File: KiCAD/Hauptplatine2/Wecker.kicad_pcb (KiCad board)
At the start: 2 copper layers, 45 parts, among them IC1 ATMEGA328P-P, P1 CONN_5V, P10 LED_Bild2, P11 CONN_MP3, P2 CONN_MP3Player, P3 LED_Bild1, P4 CONN_TASTER, P5 CONN_DREHENCODER, P6 CONN_DISPLAY, P7 CONN_01X02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

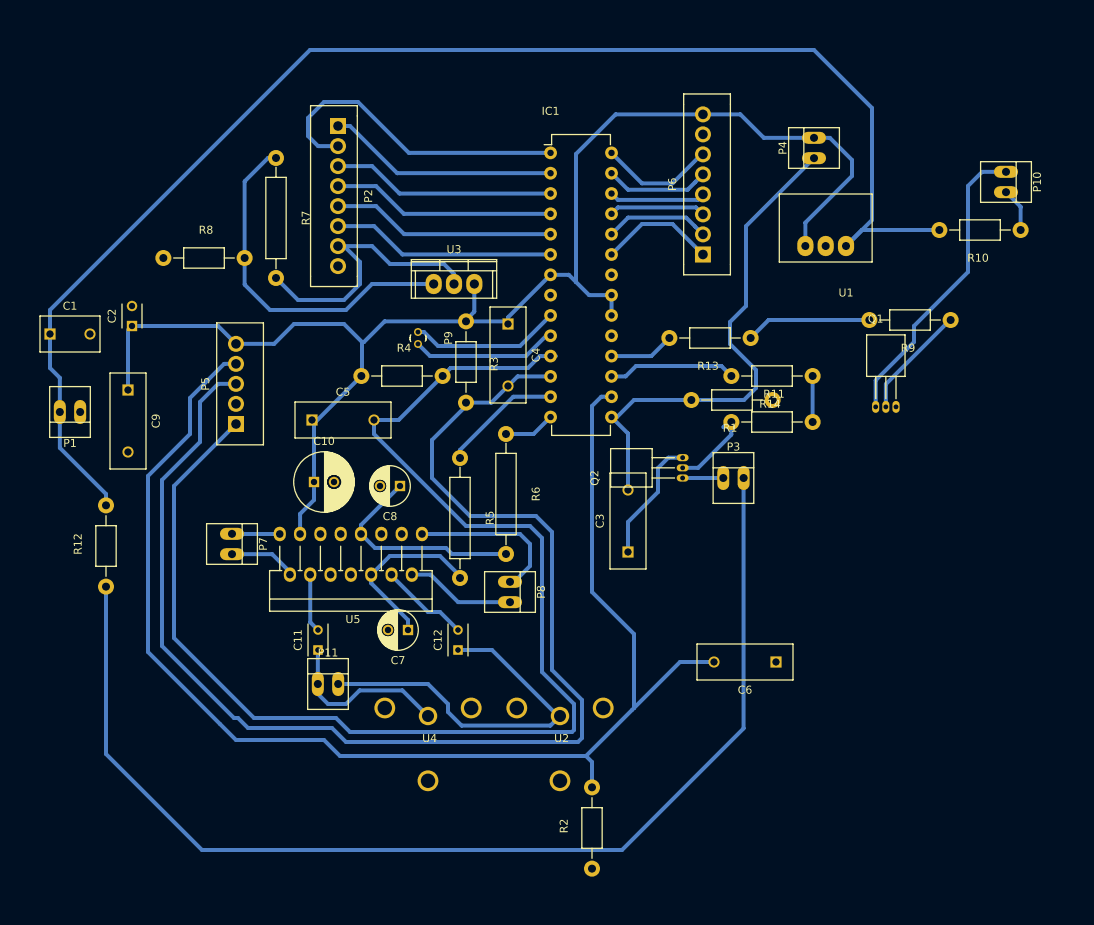
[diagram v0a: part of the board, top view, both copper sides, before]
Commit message: PCB enger gepackt. MP3 Player in Code eingebunden.
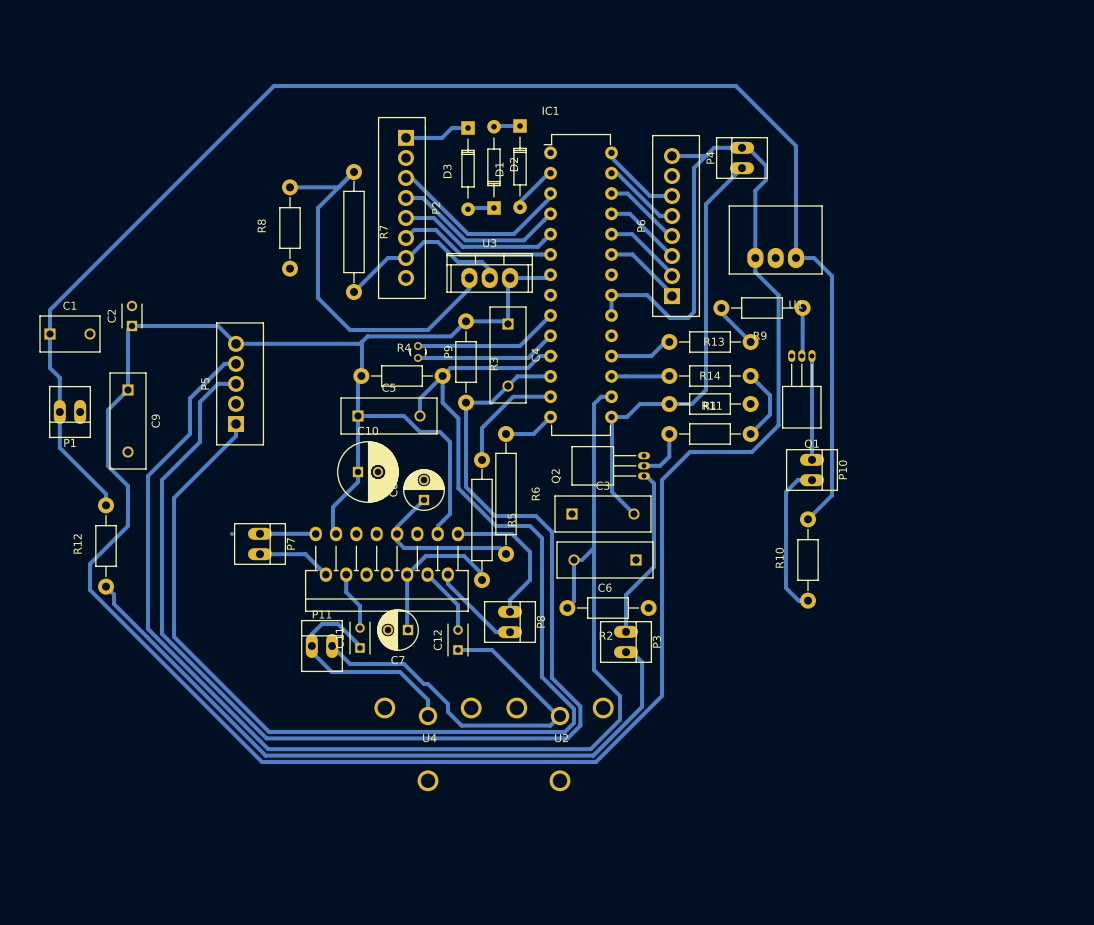
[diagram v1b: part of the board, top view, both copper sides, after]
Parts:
- added D1: D, Diodes_ThroughHole:Diode_DO-35_SOD27_Horizontal_RM10, F.Cu at (131.5, 53.2)
- added D2: D, Diodes_ThroughHole:Diode_DO-35_SOD27_Horizontal_RM10, F.Cu at (128.2, 63.5)
- added D3: D, Diodes_ThroughHole:Diode_DO-35_SOD27_Horizontal_RM10, F.Cu at (125.0, 53.5)
- moved R10 46.5 mm to (167.5, 107.5), turned to 90 degrees
- moved P10 43.4 mm to (168.0, 96.2)
- moved R2 27.6 mm to (142.5, 113.5), turned to 180 degrees
- moved P3 24.5 mm to (144.8, 117.8), turned to 270 degrees
- moved C6 21.7 mm to (146.0, 107.5)
- moved R9 18.6 mm to (161.8, 76.0)
- moved R8 11.4 mm to (102.8, 66.0), turned to 90 degrees
- moved Q1 10.2 mm to (168.0, 82.0), turned to 180 degrees
- moved R7 9.91 mm to (110.8, 66.5)
- moved P4 9.09 mm to (159.2, 57.2)
- moved P2 8.63 mm to (117.2, 54.7)
- moved C3 8.46 mm to (138.0, 101.8), turned to 0 degrees
- moved R11 7.89 mm to (155.2, 91.8)
- moved R14 7.75 mm to (155.2, 84.5)
- moved P6 6.48 mm to (150.5, 74.5)
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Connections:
- IC1 pad 1: MP3-ON2 -> Net-(IC1-Pad1)
- P2 pad 1: MP3-ON1 -> Net-(D3-Pad1)
- P2 pad 2: MP3-ON2 -> Net-(P2-Pad2)
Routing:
- net DE-E: track 180.0 -> 359.1 mm
- net Net-(P3-Pad2): track 144.5 -> 87.1 mm
- net MP3-ON2: track 40.3 -> 0.00 mm
- net Net-(P10-Pad1): track 38.1 -> 13.0 mm
- net MP3-ON1: track 29.0 -> 5.97 mm
- net Net-(P3-Pad1): track 5.08 -> 21.6 mm
- net DE-C: track 15.7 -> 0.11 mm
- net Net-(P10-Pad2): track 5.49 -> 19.3 mm
- net MP3-VCC: track 36.0 -> 22.8 mm
- net DE-D: track 169.6 -> 158.1 mm
- net Net-(R13-Pad1): track 15.8 -> 5.77 mm
- net LED-Bild1: track 16.0 -> 7.25 mm
- net MP3-T5: track 28.0 -> 19.8 mm
- net Net-(D3-Pad1): track 0.00 -> 8.26 mm
- net Net-(Q1-Pad2): track 14.3 -> 6.04 mm
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
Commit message: Haupptlatine2 fertig, Masseflächen vergrößert, Leiterbahnen zusammengeschoben
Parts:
- moved P1 98.2 mm to (167.0, 54.0), turned to 0 degrees
- moved C1 98.2 mm to (169.2, 61.2), turned to 180 degrees
- moved C2 84.5 mm to (150.5, 129.0), turned to 0 degrees
- moved R12 72.5 mm to (150.2, 122.8), turned to 0 degrees
- moved C9 71.7 mm to (151.2, 106.5), turned to 0 degrees
- moved P5 70.3 mm to (160.8, 117.8), turned to 270 degrees
- moved R10 10.4 mm to (159.2, 101.2), turned to 180 degrees
- moved P7 8.90 mm to (104.5, 98.5), turned to 180 degrees
- moved U4 2.51 mm to (117.5, 127.2)
- moved U1 1.25 mm to (166.0, 71.0)
- moved C5 1.00 mm to (112.2, 89.5)
- moved R2 1.00 mm to (143.5, 113.5)
- moved P4 0.56 mm to (158.8, 57.5)
- moved U2 0.50 mm to (136.0, 127.0)
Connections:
- P5 pad 1: DE-A -> DE-C
- P5 pad 2: DE-C -> DE-A
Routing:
- net +5V: track 186.4 -> 80.9 mm
- net Net-(P3-Pad2): track 87.1 -> 4.66 mm
- net DE-D: track 158.1 -> 84.9 mm
- net DE-B: track 156.1 -> 98.5 mm
- net DE-A: track 159.2 -> 116.5 mm
- net DE-E: track 359.1 -> 384.5 mm
- net Net-(P10-Pad2): track 19.3 -> 5.25 mm
- net SPK-R-: track 9.30 -> 13.9 mm
- net MP3-L: track 29.2 -> 26.2 mm
- net MP3-R: track 50.0 -> 52.5 mm
- net T1.1: track 57.3 -> 59.2 mm
- net Amp-Mute: track 14.2 -> 15.5 mm
- net SPK-R+: track 6.98 -> 5.86 mm
- net Net-(R7-Pad1): track 50.5 -> 49.4 mm
- net DE-C: track 0.11 -> 1.00 mm
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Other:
- board outline added: 77.5 x 90.2 mm
- rule trace_min: 0.2 -> 0.5

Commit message: Doku erweitert
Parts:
- moved C9 50.6 mm to (104.8, 86.5), turned to 90 degrees
- moved C2 42.2 mm to (162.2, 88.5)
- moved Q1 28.9 mm to (153.5, 107.0), turned to 90 degrees
- moved R9 28.5 mm to (162.8, 104.5), turned to 0 degrees
- moved P3 27.8 mm to (165.5, 99.2)
- moved R12 22.1 mm to (154.0, 101.0), turned to 180 degrees
- moved P4 21.8 mm to (151.2, 78.0)
- moved P10 13.4 mm to (165.8, 109.5)
- moved C1 13.1 mm to (165.2, 73.8)
- moved U1 12.8 mm to (167.5, 83.8)
- moved R10 11.7 mm to (152.8, 111.0)
- moved C6 10.5 mm to (135.5, 107.5), turned to 0 degrees
- moved P1 7.74 mm to (160.0, 57.2)
- moved P5 6.17 mm to (155.0, 120.0), turned to 180 degrees
- moved R13 4.42 mm to (152.0, 83.2)
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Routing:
- net DE-E: track 384.5 -> 291.6 mm
- net DE-D: track 84.9 -> 54.6 mm
- net Net-(R13-Pad1): track 5.77 -> 29.2 mm
- net T1.1: track 59.2 -> 36.8 mm
- net DE-A: track 116.5 -> 95.7 mm
- net DE-B: track 98.5 -> 78.9 mm
- net +5V: track 80.9 -> 95.0 mm
- net Net-(P10-Pad2): track 5.25 -> 13.4 mm
- net LED-Bild2: track 8.17 -> 4.49 mm
- net Net-(C7-Pad1): track 18.6 -> 21.7 mm
- net Net-(Q2-Pad2): track 6.48 -> 4.27 mm
- net LED-Bild1: track 7.25 -> 5.18 mm
- net Net-(P3-Pad2): track 4.66 -> 6.62 mm
- net Net-(Q1-Pad2): track 6.04 -> 4.68 mm
- net DISP-SCL: track 9.91 -> 8.62 mm
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
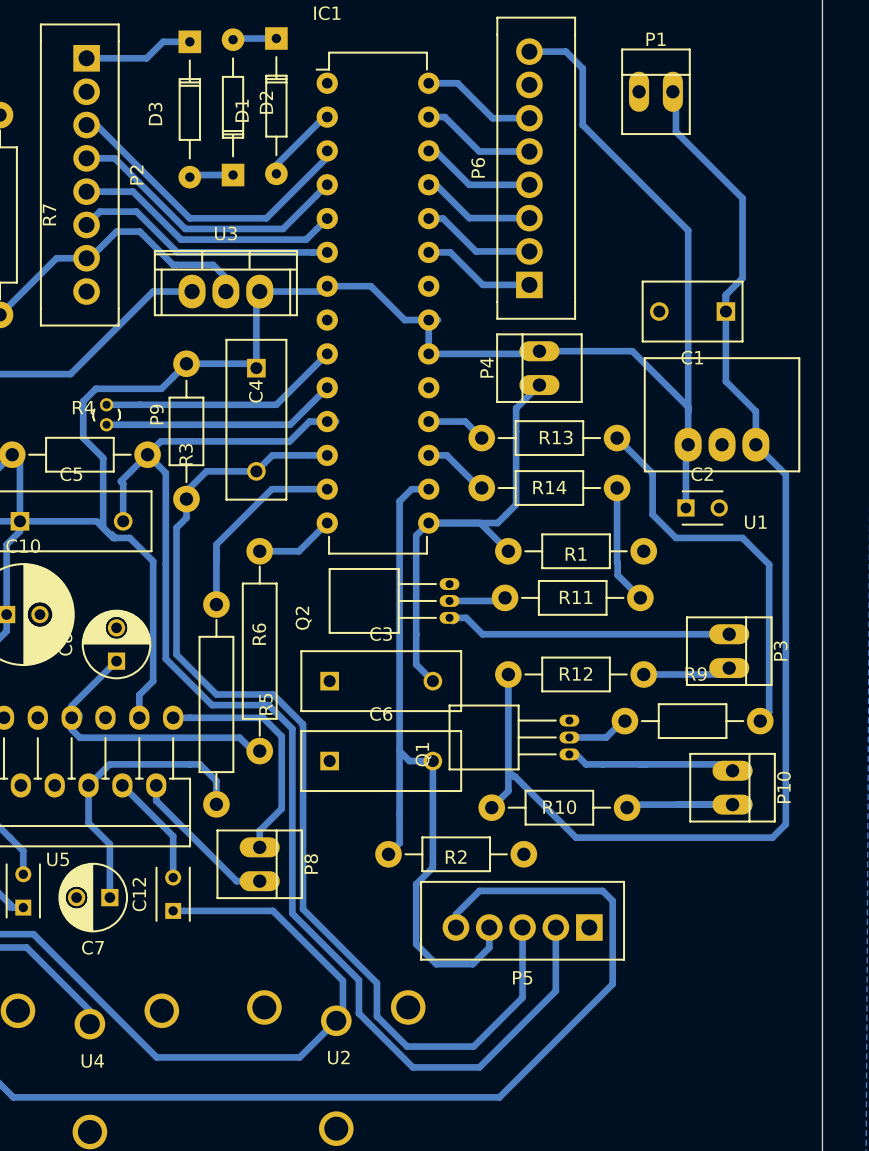
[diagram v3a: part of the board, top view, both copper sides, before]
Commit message: Doku fortgesetzt, Platine wurde hergestellt
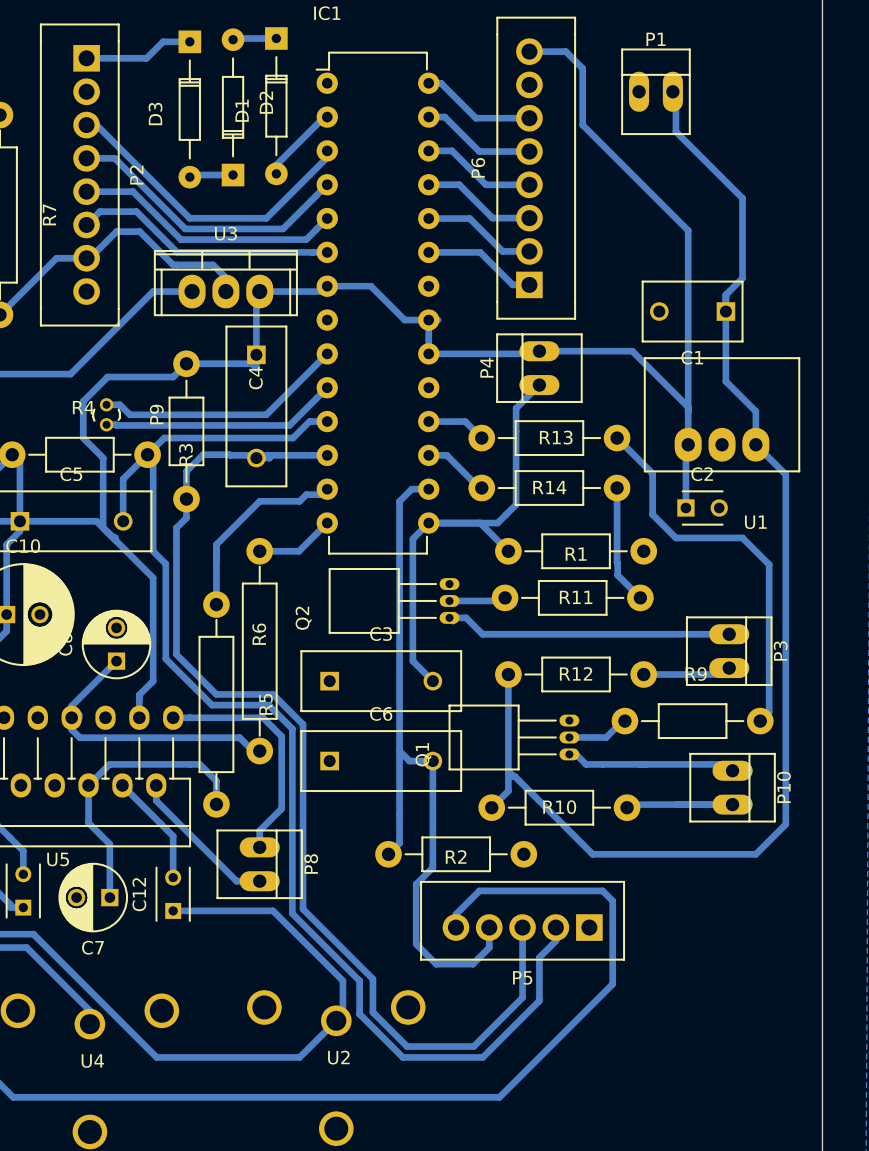
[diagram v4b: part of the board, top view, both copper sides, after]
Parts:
- moved C4 1.00 mm to (130.0, 77.0)
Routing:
- net DE-B: track 78.9 -> 81.0 mm
- net DE-A: track 95.7 -> 94.0 mm
- net +5V: track 95.0 -> 96.0 mm
- net DE-E: track 291.6 -> 290.8 mm
- net Net-(IC1-Pad9): track 18.4 -> 19.0 mm
